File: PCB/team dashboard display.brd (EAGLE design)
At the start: 160 x 100 mm, 36 parts, among them IC3 ICL7663CPA

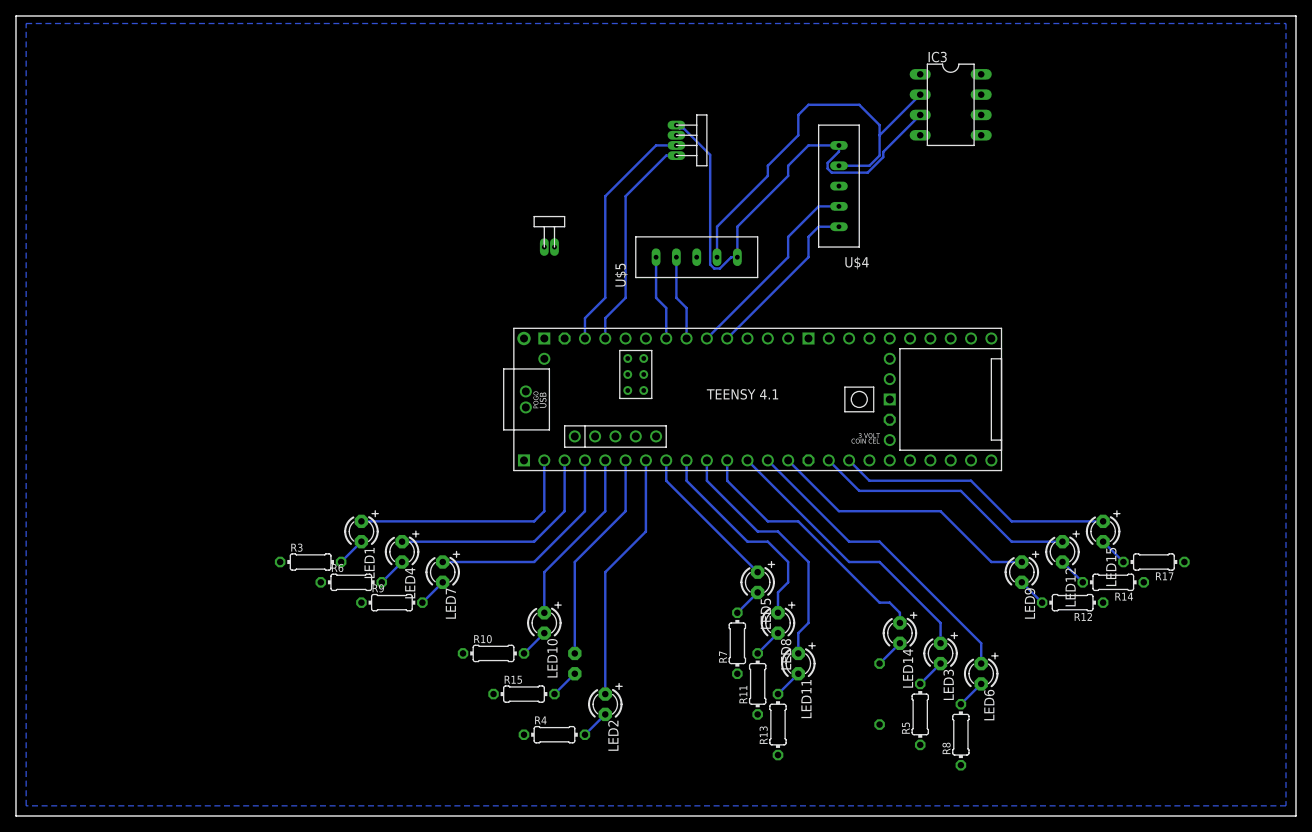
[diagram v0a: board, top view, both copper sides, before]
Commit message: added 3-pin header to dashboard display pcb/schematic. optimized component layout and shrunk pcb board by 40-50%
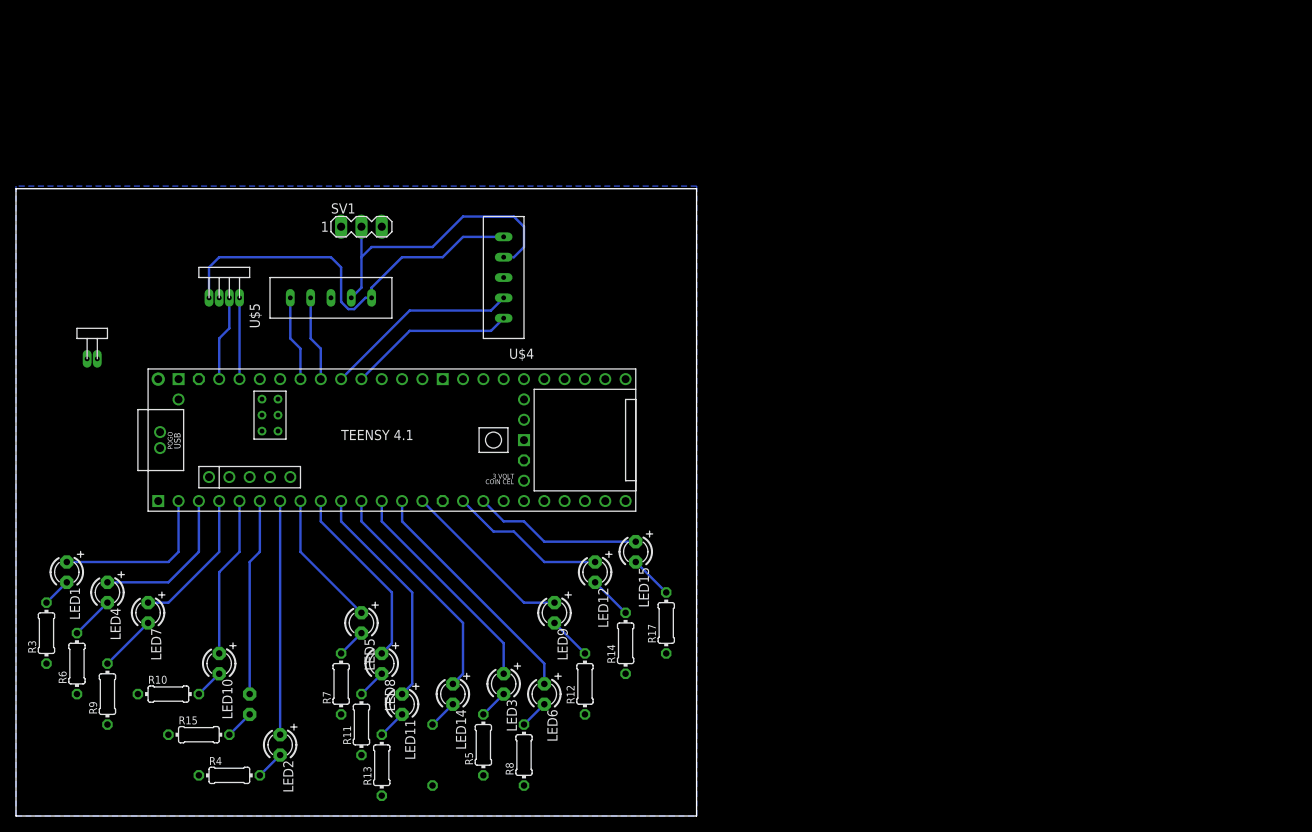
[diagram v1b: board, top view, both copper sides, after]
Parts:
- removed IC3: ICL7663CPA, maxim:DIL08
- added SV1: (no value), con-lstb:MA03-1
- moved U$9 64.9 mm to (21.6, 63.5), turned to 0 degrees
- moved R12 61.8 mm to (71.1, 16.5), turned to 90 degrees
- moved R17 61.4 mm to (81.3, 24.1), turned to 90 degrees
- moved R14 61.4 mm to (76.2, 21.6), turned to 90 degrees
- moved U$8 58.8 mm to (5.08, 54.6)
- moved LED9 58.6 mm to (67.3, 25.4)
- moved LED12 58.5 mm to (72.4, 30.5)
- moved LED15 58.5 mm to (77.5, 33.0)
- moved R16 56.4 mm to (52.1, 7.62)
- moved LED14 56.4 mm to (54.6, 15.2)
- moved R5 54.7 mm to (58.4, 8.89)
- moved LED3 54.7 mm to (61.0, 16.5)
- moved LED6 54.7 mm to (66.0, 15.2)
- moved R8 54.7 mm to (63.5, 7.62)
- moved LED11 49.8 mm to (48.3, 14.0)
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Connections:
- net 12V: now also SV1.3; no longer IC3.8
- net 3.3V: no longer IC3.3
- net 5V: now also SV1.2; no longer IC3.2
- net GND: now also SV1.1; no longer IC3.4
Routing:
- net N$13: track 30.4 -> 10.7 mm
- net N$12: track 27.3 -> 10.2 mm
- net A3-L4: track 33.4 -> 19.7 mm
- net A3-L5: track 34.9 -> 21.2 mm
- net 3.3V: track 63.7 -> 50.9 mm
- net A3-L3: track 34.5 -> 21.8 mm
- net 5V: track 50.3 -> 38.0 mm
- net A1-L3: track 26.8 -> 17.9 mm
- net A1-L1: track 29.7 -> 20.8 mm
- net A1-L2: track 28.2 -> 19.4 mm
- net A3-L2: track 38.7 -> 30.2 mm
- net A3-L1: track 35.1 -> 27.9 mm
- net N$18: track 3.59 -> 7.18 mm
- net A2-L5: track 32.2 -> 28.6 mm
- net A2-L3: track 26.3 -> 23.3 mm
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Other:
- board size 160 x 100 mm -> 85.1 x 78.4 mm
